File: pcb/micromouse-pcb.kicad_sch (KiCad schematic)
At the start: 49 parts, among them J1 Conn_01x08, J1_MotorEncoder1 Conn_01x06, J2_MotorEncoder1 Conn_01x06, J3 Conn_01x08, J4 Conn_01x08, Q1 BS170, Q2 TEFT4300, Q3 BS170, Q4 TEFT4300, Q5 BS170, Q6 TEFT4300, Q7 BS170, Q8 TEFT4300, SW1 SW_SPDT, U0 Teensy 4.1, U2 L7805

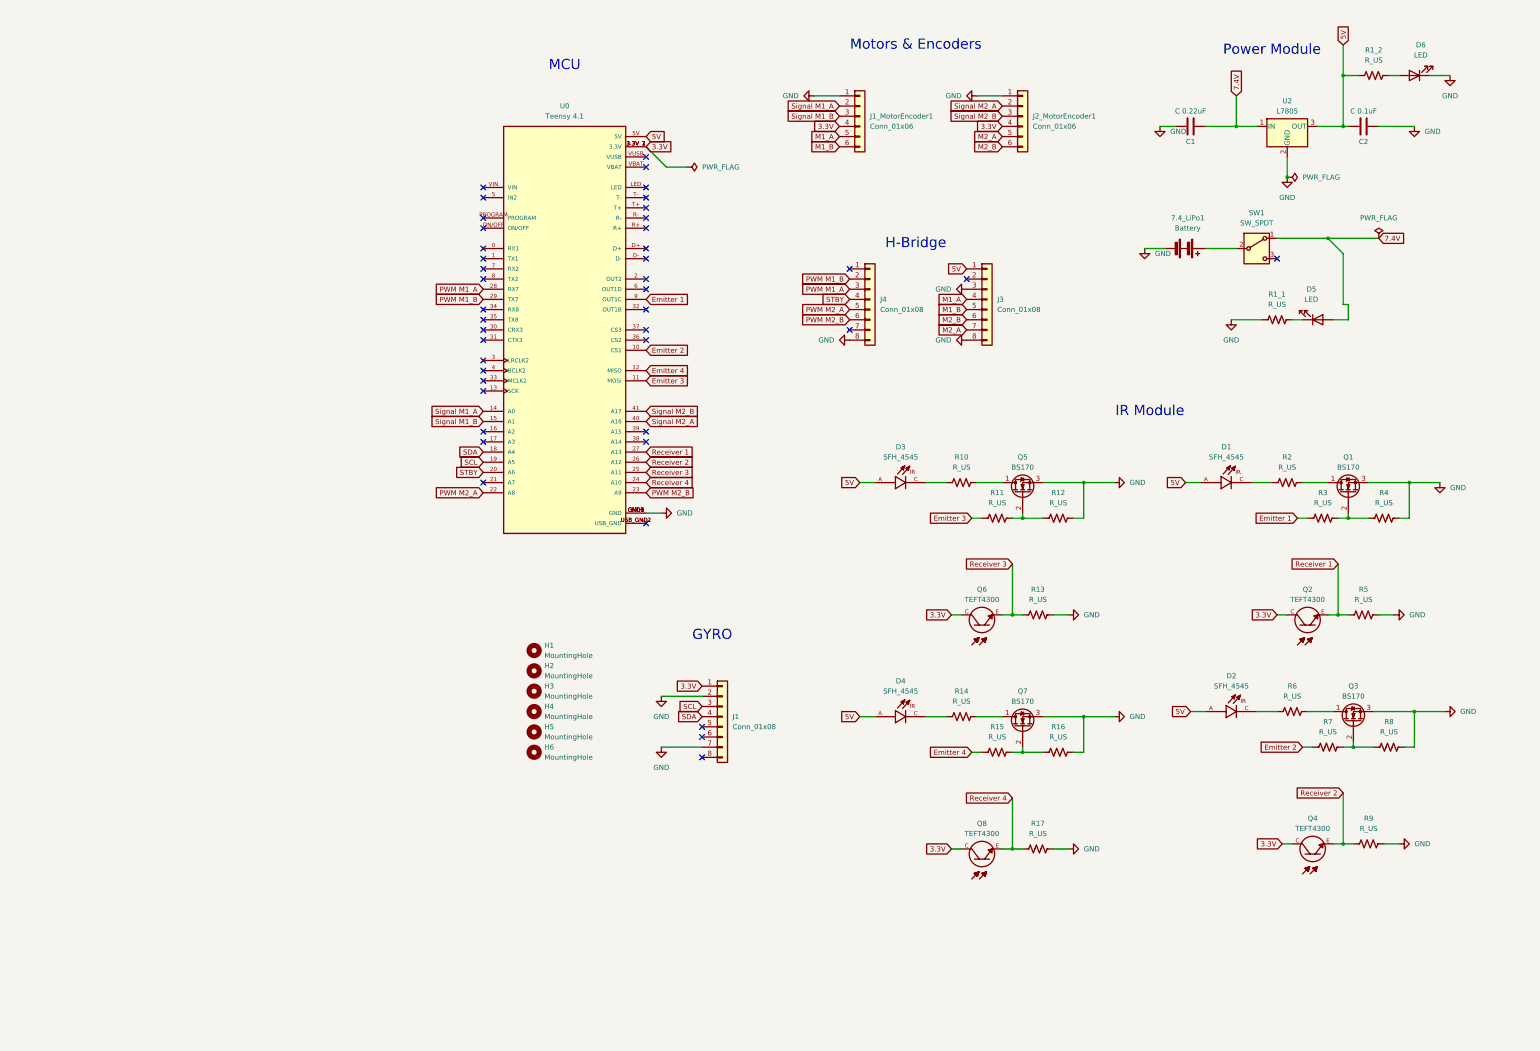
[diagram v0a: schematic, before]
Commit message: Reformatted schematic; Fixed Teensy & IR footprints; Changed Board Setups
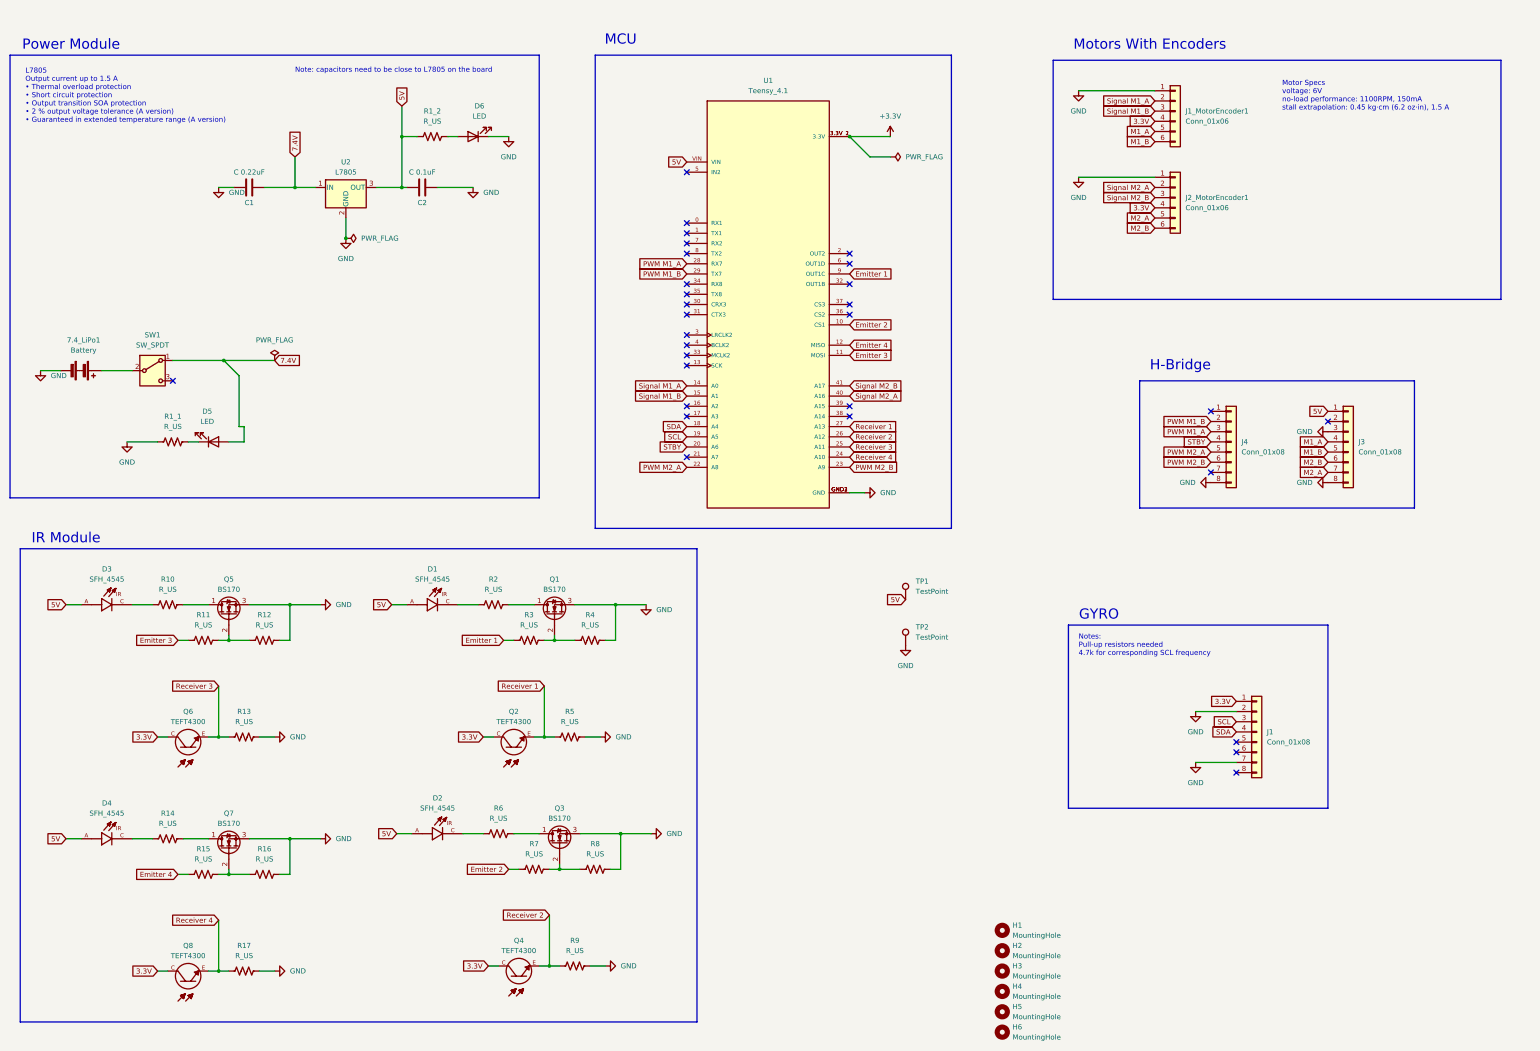
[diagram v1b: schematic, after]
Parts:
- removed U0: Teensy 4.1, DEV-16771:MODULE_DEV-16771, symbol Teensy 4.1:DEV-16771
- added TP1, TP2: TestPoint, TestPoint:TestPoint_THTPad_D1.5mm_Drill0.7mm, symbol Connector:TestPoint
- added U1: Teensy_4.1, micromouse:Teensy4.1_LessHoles, symbol micromouse-symbols:Teensy_4.1
- D1, D2, D3, D4: footprint SFH_4545:DIO_SFH_4545 -> micromouse:LED_D5.0mm_IR
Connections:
- net 5V: now also TP1.1, U1.VIN
- net Emitter 1: now also U1.9 (OUT1C)
- net Emitter 2: now also U1.10 (CS1)
- net Emitter 3: now also U1.11 (MOSI)
- net Emitter 4: now also U1.12 (MISO)
- net GND: now also TP2.1, U1.GND1 (GND), U1.GND2 (GND), U1.GND3 (GND)
- net PWM M1_A: now also U1.28 (RX7)
- net PWM M1_B: now also U1.29 (TX7)
- net PWM M2_A: now also U1.22 (A8)
- net PWM M2_B: now also U1.23 (A9)
- net Receiver 1: now also U1.27 (A13)
- net Receiver 2: now also U1.26 (A12)
- net Receiver 3: now also U1.25 (A11)
- net Receiver 4: now also U1.24 (A10)
- net SCL: now also U1.19 (A5)
- net SDA: now also U1.18 (A4)
- net STBY: now also U1.20 (A6)
- net Signal M1_A: now also U1.14 (A0)
- net Signal M1_B: now also U1.15 (A1)
- net Signal M2_A: now also U1.40 (A16)
- net Signal M2_B: now also U1.41 (A17)
- new net +3.3V: U1.3.3V_1 (3.3V), U1.3.3V_2 (3.3V)
- no-connect marks 43 -> 30
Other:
- note added: "L7805 Output current up to 1.5 A • Thermal overload protection • Short circuit protection • Output transition SOA protection • 2 % output voltage tolerance (A version) • Guaranteed in extended temperature range (A version)"
- note added: "Motor Specs voltage: 6V no-load performance: 1100RPM, 150mA stall extrapolation: 0.45 kg⋅cm (6.2 oz⋅in), 1.5 A"
- note added: "Motors With Encoders"
- note added: "Note: capacitors need to be close to L7805 on the board"
- note added: "Notes: Pull-up resistors needed 4.7k for corresponding SCL frequency"
- note removed: "Motors & Encoders"
- company: (none) -> Roboracing
- title: (none) -> Micromouse
- moved on the sheet: 7.4_LiPo1, C1, C2, D1, D2, D3, D4, D5, D6, H1, H2, H3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

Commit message: Done placement
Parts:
- removed R1_1: R_US, Resistor_SMD:R_1206_3216Metric_Pad1.30x1.75mm_HandSolder, symbol Device:R_US
- removed SW1: SW_SPDT, Connector_PinHeader_2.54mm:PinHeader_1x03_P2.54mm_Vertical, symbol Switch:SW_SPDT
- added C3: C, Capacitor_SMD:C_1206_3216Metric_Pad1.33x1.80mm_HandSolder, symbol Device:C
- added Q9: FQP27P06, Package_TO_SOT_THT:TO-220-3_Vertical, symbol Transistor_FET:FQP27P06
- added R1, R18: R_US, Resistor_SMD:R_1206_3216Metric_Pad1.30x1.75mm_HandSolder, symbol Device:R_US
- added R19, R20: 4.7k, Resistor_SMD:R_1206_3216Metric_Pad1.30x1.75mm_HandSolder, symbol Device:R_US
- added R21: 1k, Resistor_SMD:R_1206_3216Metric_Pad1.30x1.75mm_HandSolder, symbol Device:R_US
- added SW2: SW_SPDT, Button_Switch_THT:SW_Slide_SPDT_Angled_CK_OS102011MA1Q, symbol Switch:SW_SPDT
- added TP3, TP4, TP5, TP6: TestPoint, micromouse:TestPoint_THTPad_D2.0mm_Drill1.0mm, symbol Connector:TestPoint
- 7.4_LiPo1: footprint Connector_PinHeader_2.54mm:PinHeader_1x02_P2.54mm_Vertical -> Connector_JST:JST_PH_B2B-PH-K_1x02_P2.00mm_Vertical
- D1, D2, D3, D4: footprint micromouse:LED_D5.0mm_IR -> micromouse:DIO_SFH_4545_copy
- D5, D6: footprint LED_THT:LED_D5.0mm -> LED_SMD:LED_1206_3216Metric_Pad1.42x1.75mm_HandSolder
- R2: value R_US -> 100/75
- R3: value R_US -> 1.3k
- R4: value R_US -> 2k
- TP1, TP2: footprint TestPoint:TestPoint_THTPad_D1.5mm_Drill0.7mm -> micromouse:TestPoint_THTPad_D2.0mm_Drill1.0mm
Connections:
- net 3.3V: now also R19.1, R20.1, TP3.1, TP4.1
- net 5V: now also C2.2; no longer C2.1
- net 7.4V: now also Q9.2 (D); no longer D5.2 (A)
- net Emitter 1: now also U1.38 (A14); no longer U1.9 (OUT1C)
- net Emitter 2: now also U1.39 (A15); no longer U1.10 (CS1)
- net Emitter 3: now also U1.40 (A16); no longer U1.11 (MOSI)
- net Emitter 4: now also U1.41 (A17); no longer U1.12 (MISO)
- net GND: now also C2.1, D5.1 (K), C3.2, SW2.3 (C); no longer C2.2
- net SCL: now also R20.2
- net SDA: now also R19.2
- net at U1.0 (RX1): now also R21.2
- net ENC_M1_A: now reaches U1.34 (RX8)
- net ENC_M1_A: now also J1_MotorEncoder1.2 (Pin_2)
- net ENC_M1_B: now reaches U1.35 (TX8)
- net ENC_M1_B: now also J1_MotorEncoder1.3 (Pin_3)
- net ENC_M2_A: now reaches U1.36 (CS2)
- net ENC_M2_A: now also J2_MotorEncoder1.2 (Pin_2)
- net ENC_M2_B: now reaches U1.37 (CS3)
- net ENC_M2_B: now also J2_MotorEncoder1.3 (Pin_3)
- net at 7.4_LiPo1.1 (+): now also Q9.3 (S), R1.1
- net at J3.2 (Pin_2): now also TP5.1, TP6.1
- net PWMA_6612: now reaches J4.1 (Pin_1)
- net PWMA_6612: now also U1.11 (MOSI)
- net PWMB_6612: now reaches J4.7 (Pin_7)
- net PWMB_6612: now also U1.12 (MISO)
- net M1_A renamed POW_M1_A
- net M1_B renamed POW_M1_B
- net M2_A renamed POW_M2_A
- net M2_B renamed POW_M2_B
- net Signal M1_A: no longer names the net of U1.14 (A0)
- net Signal M1_A: no longer J1_MotorEncoder1.2 (Pin_2)
- net Signal M1_B: no longer names the net of U1.15 (A1)
- net Signal M1_B: no longer J1_MotorEncoder1.3 (Pin_3)
- removed net Signal M2_A: J2_MotorEncoder1.2 (Pin_2), U1.40 (A16)
- removed net Signal M2_B: J2_MotorEncoder1.3 (Pin_3), U1.41 (A17)
- new net: C3.1, Q9.1 (G), R1.2, R18.1
- new net: R18.2, SW2.2 (B)
- new net: D5.2 (A), R21.1
- no-connect marks 30 -> 24
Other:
- note added: "Note: The pins labeled PWM6612 are for compatibility with the TB6612FNG H-bridge. When choosing TB6612FNG, solder a jumper wire from the pin to 3.3V through the test points."
- moved on the sheet: C1, C2, D6, H1, H2, H3, H4, H5, H6, J1, J1_MotorEncoder1, J2_MotorEncoder1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

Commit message: Finished Routing!
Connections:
- net 3.3V is gone; now on net +3.3V: J1.1 (Pin_1), J1_MotorEncoder1.4 (Pin_4), J2_MotorEncoder1.4 (Pin_4), Q2.C, Q4.C, Q6.C, Q8.C, R19.1, R20.1, TP3.1, TP4.1
- net ENC_M1_A: now also U1.36 (CS2); no longer U1.34 (RX8)
- net ENC_M1_B: now also U1.37 (CS3); no longer U1.35 (TX8)
- net ENC_M2_A: now also U1.34 (RX8); no longer U1.36 (CS2)
- net ENC_M2_B: now also U1.35 (TX8); no longer U1.37 (CS3)
- net Emitter 1: now also U1.25 (A11); no longer U1.38 (A14)
- net Emitter 2: now also U1.40 (A16); no longer U1.39 (A15)
- net Emitter 3: now also U1.39 (A15); no longer U1.40 (A16)
- net Emitter 4: now also U1.26 (A12); no longer U1.41 (A17)
- net PWMA_6612: now also U1.15 (A1); no longer U1.11 (MOSI)
- net PWMB_6612: now also U1.14 (A0); no longer U1.12 (MISO)
- net Receiver 1: now also U1.24 (A10); no longer U1.27 (A13)
- net Receiver 2: now also U1.41 (A17); no longer U1.26 (A12)
- net Receiver 3: now also U1.38 (A14); no longer U1.25 (A11)
- net Receiver 4: now also U1.27 (A13); no longer U1.24 (A10)
- net 5V renamed +5V
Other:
- moved on the sheet: C1, C2, D6, J1_MotorEncoder1, J2_MotorEncoder1, R19, R1_2, R20, TP1, TP2, TP3, TP4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

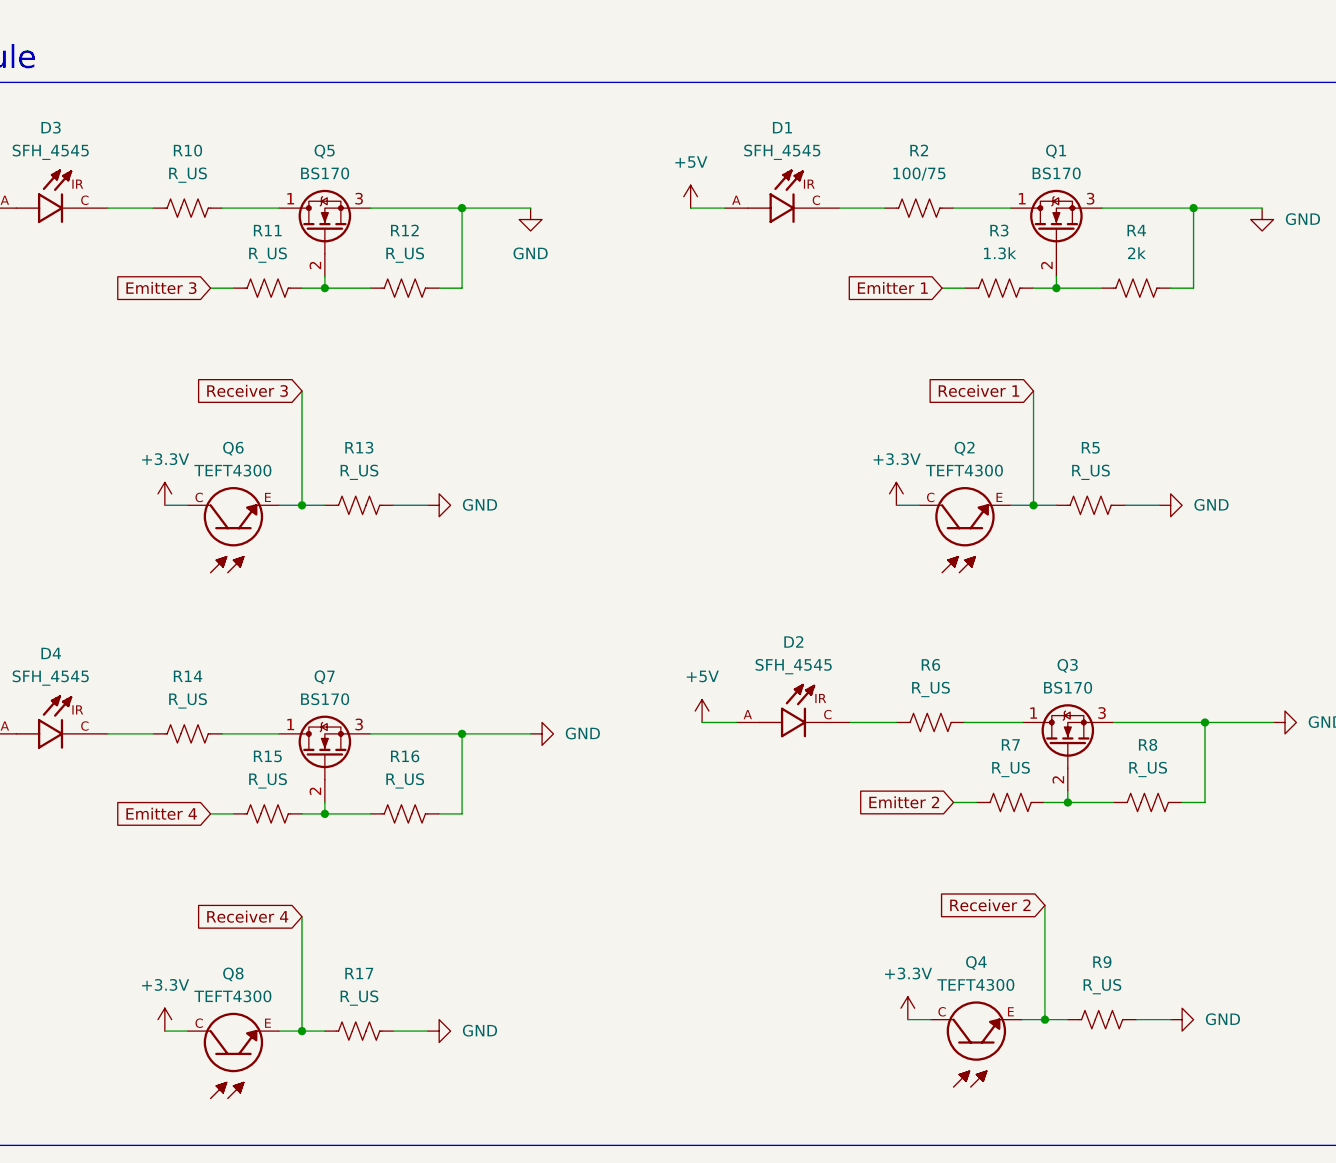
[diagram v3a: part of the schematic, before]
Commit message: updated resistor values on schematic
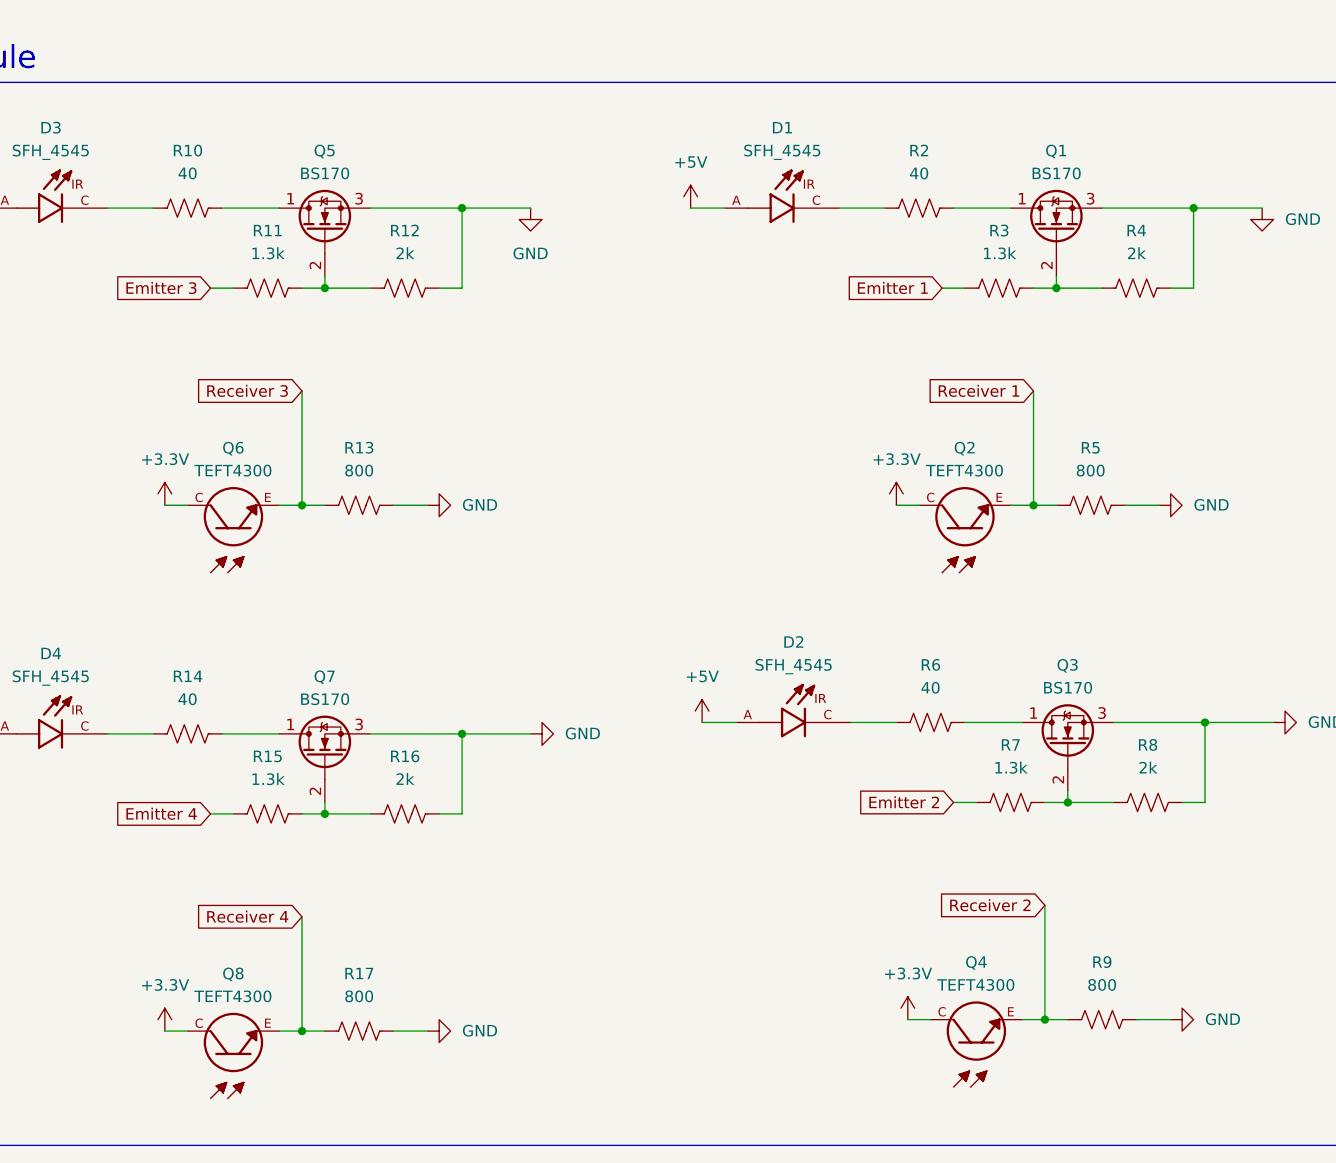
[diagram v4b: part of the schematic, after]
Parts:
- R10, R14, R6: value R_US -> 40
- R11, R15, R7: value R_US -> 1.3k
- R12, R16, R8: value R_US -> 2k
- R13, R17, R5, R9: value R_US -> 800
- R2: value 100/75 -> 40
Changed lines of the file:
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@@
 			)
 		)
-		(property "Value" "R_US"
+		(property "Value" "2k"
 			(at 91.44 171.45 90)
 			(effects
@@
 			)
 		)
-		(property "Value" "R_US"
+		(property "Value" "800"
 			(at 86.36 195.58 90)
 			(effects
@@
 			)
 		)
-		(property "Value" "100/75"
+		(property "Value" "40"
 			(at 148.59 162.56 90)
 			(effects
@@
 			)
 		)
-		(property "Value" "R_US"
+		(property "Value" "2k"
 			(at 173.99 228.6 90)
 			(effects
@@
 			)
 		)
-		(property "Value" "R_US"
+		(property "Value" "1.3k"
 			(at 76.2 229.87 90)
 			(effects
@@
 			)
 		)
-		(property "Value" "R_US"
+		(property "Value" "40"
 			(at 67.31 162.56 90)
 			(effects
@@
 			)
 		)
-		(property "Value" "R_US"
+		(property "Value" "1.3k"
 			(at 76.2 171.45 90)
 			(effects
@@
 			)
 		)
-		(property "Value" "R_US"
+		(property "Value" "2k"
 			(at 91.44 229.87 90)
 			(effects
@@
 			)
 		)
-		(property "Value" "R_US"
+		(property "Value" "800"
 			(at 167.64 195.58 90)
 			(effects
@@
 			)
 		)
-		(property "Value" "R_US"
+		(property "Value" "800"
 			(at 86.36 254 90)
 			(effects
@@
 			)
 		)
-		(property "Value" "R_US"
+		(property "Value" "40"
 			(at 67.31 220.98 90)
 			(effects
@@
 			)
 		)
-		(property "Value" "R_US"
+		(property "Value" "1.3k"
 			(at 158.75 228.6 90)
 			(effects
@@
 			)
 		)
-		(property "Value" "R_US"
+		(property "Value" "800"
 			(at 168.91 252.73 90)
 			(effects
@@
 			)
 		)
-		(property "Value" "R_US"
+		(property "Value" "40"
 			(at 149.86 219.71 90)
 			(effects
